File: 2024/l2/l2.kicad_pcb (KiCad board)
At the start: 2 copper layers, 175 x 169.4 mm, 37 parts, among them J1 Conn_01x04, J2 Conn_01x02, J3 Conn_01x04, J4 Conn_01x02, J5 Conn_01x02, J6 Conn_01x02, J7 Conn_01x02, Q1 IRF540N, Q2 IRF540N, Q3 IRF540N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

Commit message: final 0.9
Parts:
- added R1: 3.3k, Resistor_SMD:R_0603_1608Metric_Pad0.98x0.95mm_HandSolder, F.Cu at (124.0, 179.2)
- J1, J2: moved to B.Cu
- moved U5 229.9 mm to (109.8, 169.8)
- moved J1 178.9 mm to (96.2, 178.0), turned to 90 degrees
- moved Q3 173.7 mm to (96.7, 152.4), turned to 41 degrees
- moved C3 172.0 mm to (92.3, 156.6), turned to -140 degrees
- moved J3 166.8 mm to (127.4, 166.2)
- moved Q4 166.8 mm to (119.9, 148.1), turned to -41 degrees
- moved U3 165.4 mm to (89.4, 137.6), turned to 130.5 degrees
- moved J6 152.1 mm to (104.4, 127.2), turned to -139 degrees
- moved C2 141.7 mm to (93.3, 48.1), turned to 140 degrees
- moved C4 137.9 mm to (127.2, 156.4), turned to -40 degrees
- moved U2 136.6 mm to (91.8, 65.3), turned to -130 degrees
- moved Q2 134.2 mm to (102.3, 54.8), turned to 140 degrees
- moved SW1 128.7 mm to (127.6, 181.9)
- moved U4 126.9 mm to (130.5, 137.1), turned to 49.5 degrees
- moved J5 123.7 mm to (101.2, 74.8), turned to -40 degrees
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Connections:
- SW1 pad 1: +5V -> Net-(SW1-A)
- U5 pad 0: /RXL1 -> /RXL3
- U5 pad 1: /TXL1 -> /TXL3
- U5 pad 10: INA_3 -> INA_4
- U5 pad 11: INB_3 -> PWM_4
- U5 pad 12: PWM_3 -> INB_4
- U5 pad 13: INA_4 -> INB_3
- U5 pad 14: INB_4 -> PWM_3
- U5 pad 15: PWM_4 -> INA_3
- U5 pad 17: unconnected-(U5-Pad17) -> INA_2
- U5 pad 18: unconnected-(U5-Pad18) -> PWM_2
- U5 pad 19: unconnected-(U5-Pad19) -> INB_2
- U5 pad 2: INA_1 -> unconnected-(U5-Pad2)
- U5 pad 20: unconnected-(U5-Pad20) -> /TXL1
- U5 pad 21: unconnected-(U5-Pad21) -> /RXL1
- U5 pad 3: INB_1 -> unconnected-(U5-Pad3)
- U5 pad 4: PWM_1 -> unconnected-(U5-Pad4)
- U5 pad 5: INA_2 -> INB_1
- U5 pad 6: INB_2 -> PWM_1
- U5 pad 7: /RXL3 -> unconnected-(U5-Pad7)
- U5 pad 8: /TXL3 -> unconnected-(U5-Pad8)
- U5 pad 9: PWM_2 -> INA_1
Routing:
- net /Motor Driver/MD: track 5.94 -> 380.5 mm, vias 0 -> 5
- net +12V: track 176.9 -> 336.4 mm, vias 0 -> 3
- net INB_1: track 0.00 -> 136.1 mm, vias 0 -> 1
- net PWM_1: track 0.00 -> 130.9 mm, vias 0 -> 1
- net INB_2: track 0.00 -> 123.0 mm, vias 0 -> 1
- net PWM_2: track 0.00 -> 119.4 mm, vias 0 -> 1
- net INA_1: track 0.00 -> 116.9 mm, vias 0 -> 1
- net INA_2: track 0.00 -> 114.0 mm, vias 0 -> 1
- net +5V: track 0.00 -> 69.4 mm
- net INA_4: track 0.00 -> 33.6 mm, vias 0 -> 1
- net PWM_4: track 0.00 -> 29.8 mm, vias 0 -> 1
- net INB_4: track 0.00 -> 27.8 mm, vias 0 -> 1
- net /RXL3: track 0.00 -> 23.8 mm
- net PWM_3: track 0.00 -> 20.4 mm, vias 0 -> 1
- net /TXL3: track 0.00 -> 20.3 mm
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- added copper zone on B.Cu, net +12V
- added copper zone on F.Cu, net Net-(J5-Pin_1)
- added copper zone on F.Cu, net Net-(J5-Pin_2)
- added copper zone on F.Cu, net Net-(J6-Pin_1)
- added copper zone on F.Cu, net Net-(J6-Pin_2)
- added copper zone on F.Cu, net Net-(J7-Pin_1)
- added copper zone on F.Cu, net Net-(J7-Pin_2)
- added copper zone on F.Cu, net Net-(Q2-D)
- added copper zone on F.Cu, net Net-(Q3-D)
- added copper zone on F.Cu, net Net-(Q4-D)
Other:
- outline, holes or cut-outs redrawn

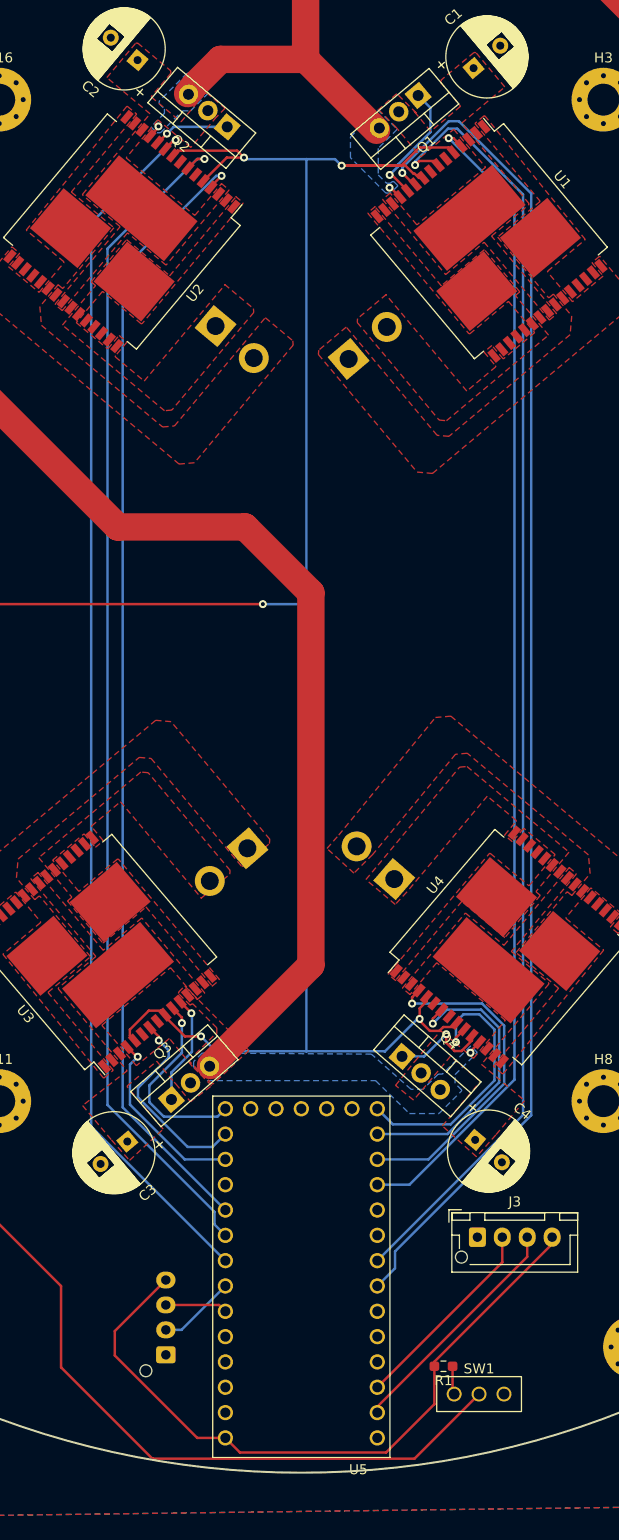
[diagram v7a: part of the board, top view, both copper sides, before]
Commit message: final 0.91
fixed:
switched analog signal pin on l1 esp32c3 to a0 since a1 not working
silkscreen is now properly placed
traces are adjusted on l1
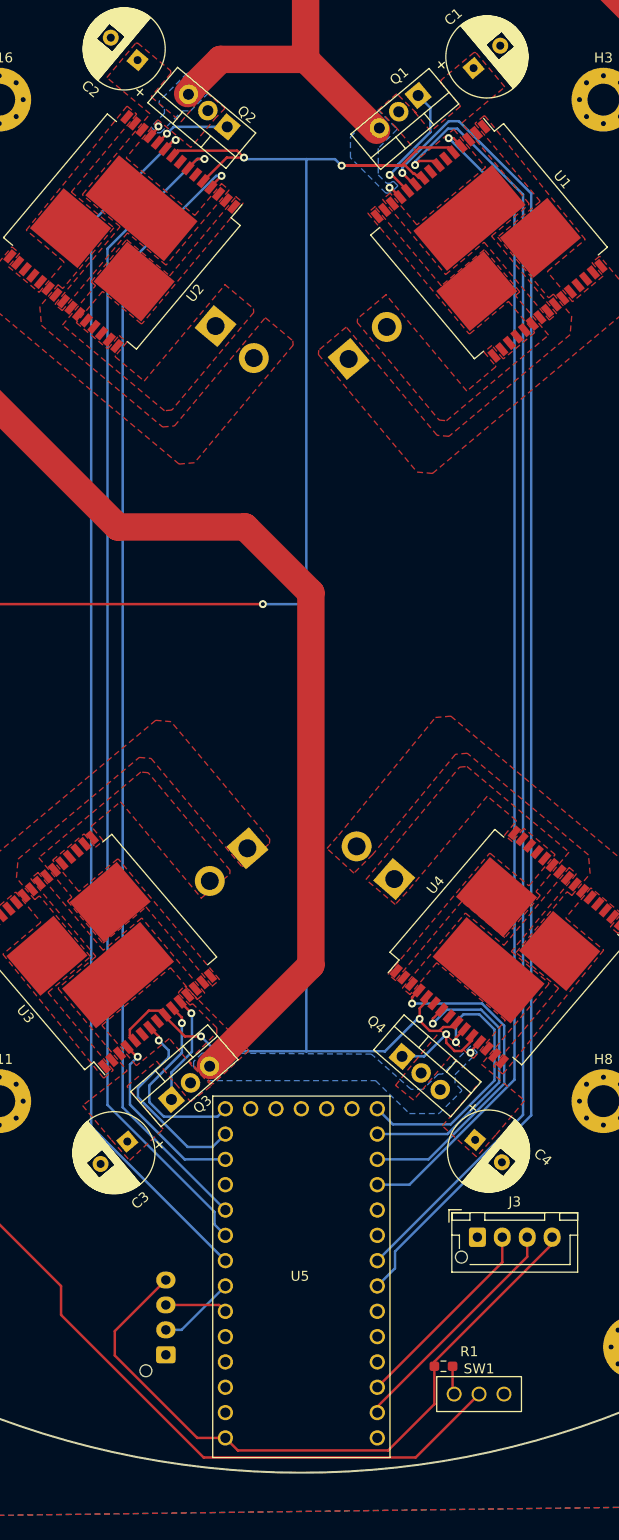
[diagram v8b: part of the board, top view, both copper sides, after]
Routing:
- net /Motor Driver/MD: track 380.5 -> 377.3 mm
